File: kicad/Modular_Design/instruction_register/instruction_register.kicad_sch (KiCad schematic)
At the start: 7 parts

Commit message: PD 70% impl
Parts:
- added J?: /implied, symbol Connector_Generic:Conn_01x01
- added J?: d, symbol Connector_Generic:Conn_01x08
- added J?: 0/ir, symbol Connector_Generic:Conn_01x01
- added J?: /twocycle, symbol Connector_Generic:Conn_01x01
- added U?: 4002, symbol 4xxx:4002
- added U? (x3): 74LS27, symbol 74xx:74LS27
- added U? (x6): 74LS04, symbol 74xx:74LS04
- added U?: 74AHC240, symbol 74xx:74AHC240
- added U?: 4081, symbol 4xxx:4081
- added U?: 4011, symbol 4xxx:4011
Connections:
- net GND: now also U?.10 (GND), U?.1 (1OE), U?.10 (GND), U?.19 (2OE)
- net at U?.1 (OE): now also J?.1 (Pin_1)
- net at U?.11 (Load): now also J?.1 (Pin_1)
- net at U?.12 (Q7): now also U?.1, U?.11 (2A3), U?.13
- net at U?.13 (Q6): now also U?.13 (2A2)
- net at U?.14 (Q5): now also U?.15 (2A1)
- net at U?.15 (Q4): now also U?.17 (2A0), U?.2, U?.5
- net at U?.16 (Q3): now also U?.1, U?.1, U?.8 (1A3)
- net at U?.17 (Q2): now also U?.2, U?.3, U?.6 (1A2)
- net at U?.18 (Q1): now also U?.1, U?.4 (1A1)
- net at U?.19 (Q0): now also U?.1, U?.1, U?.2 (1A0)
- net at U?.2 (D0): now also J?.1 (Pin_1)
- net +5V: now reaches U?.20 (VCC)
- net +5V: now also U?.20 (VCC), U?.20 (VCC)
- net at U?.3 (D1): now also J?.2 (Pin_2)
- net at U?.4 (D2): now also J?.3 (Pin_3)
- net at U?.5 (D3): now also J?.4 (Pin_4)
- net at U?.6 (D4): now also J?.5 (Pin_5)
- net at U?.7 (D5): now also J?.6 (Pin_6)
- net at U?.8 (D6): now also J?.7 (Pin_7)
- net at U?.9 (D7): now also J?.8 (Pin_8)
- net at U?.2 (D0): now also U?.18 (1Y0)
- net at U?.3 (D1): now also U?.16 (1Y1)
- net at U?.4 (D2): now also U?.14 (1Y2)
- net at U?.5 (D3): now also U?.12 (1Y3)
- net at U?.6 (D4): now also U?.3 (2Y0)
- net at U?.7 (D5): now also U?.5 (2Y1)
- net at U?.8 (D6): now also U?.7 (2Y2)
- net at U?.9 (D7): now also U?.9 (2Y3)
- new net: U?.1, U?.1
- new net: U?.2, U?.2 (x2)
- new net: U?.2, U?.4
- new net: J?.1 (Pin_1), U?.2
- new net: U?.1, U?.12
- new net: U?.1, U?.1, U?.12
- new net: U?.13, U?.2
- new net: U?.1, U?.3
- new net: J?.1 (Pin_1), U?.3
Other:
- moved on the sheet: J?, U?, U?A

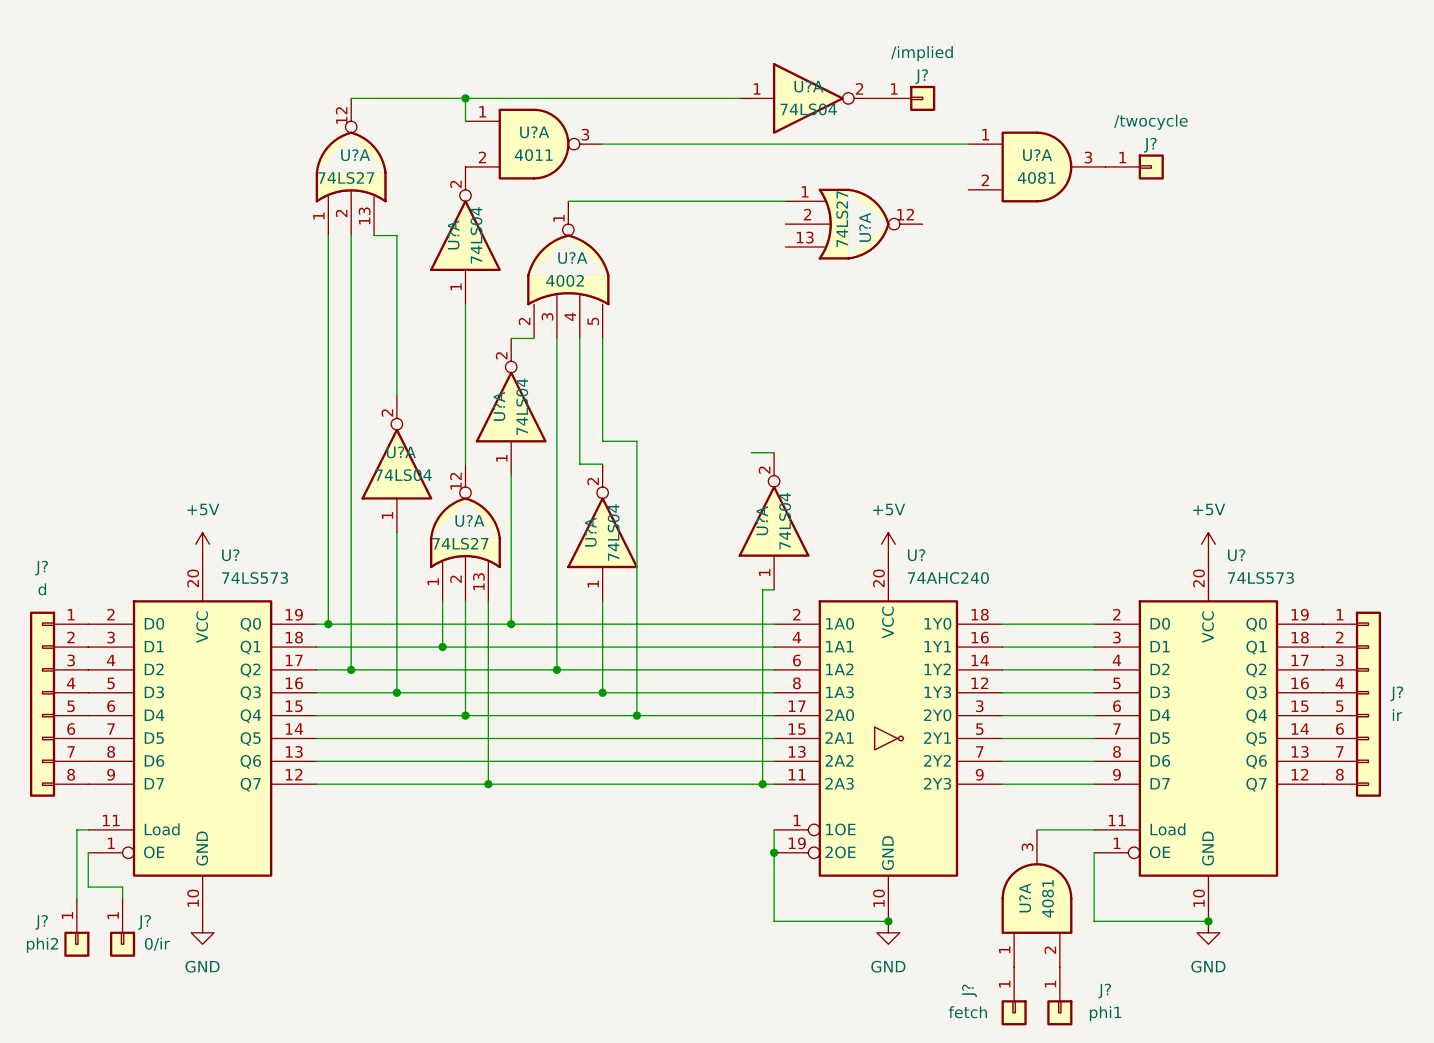
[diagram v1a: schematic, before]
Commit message: finish logic gates between ir and predecoder
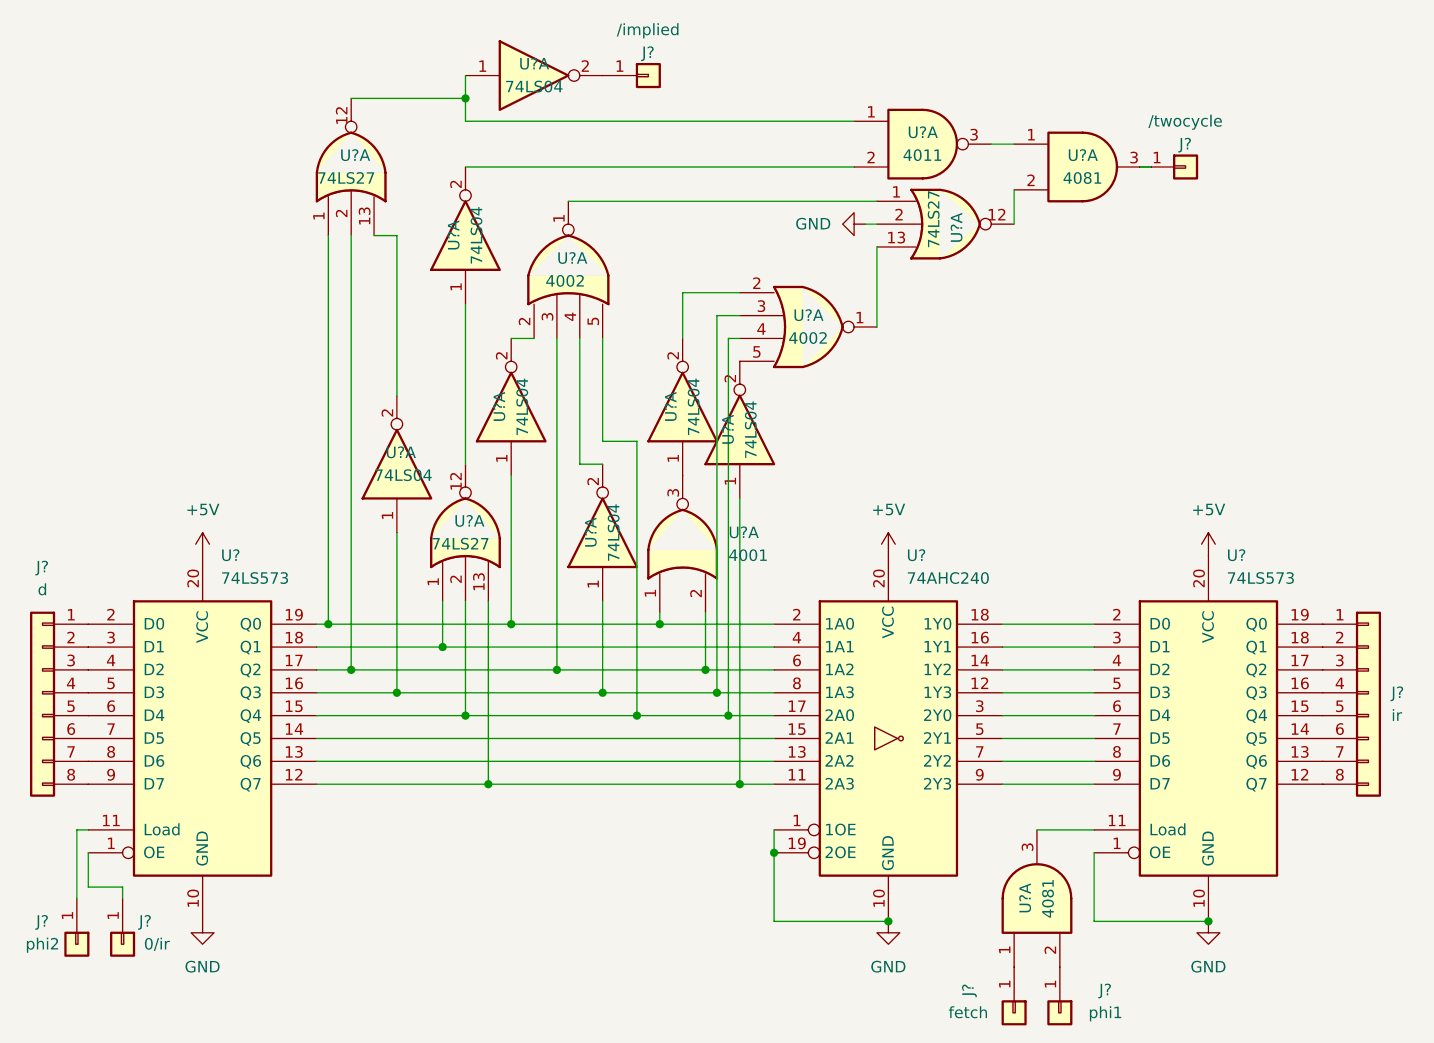
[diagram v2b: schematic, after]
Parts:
- removed U?: 74LS04, symbol 74xx:74LS04
- added U? (x2): 74LS04, symbol 74xx:74LS04
- added U?: 4002, symbol 4xxx:4002
- added U?: 4001, symbol 4xxx:4001
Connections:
- net GND: now also U?.2
- net at U?.17 (Q2), U?.2, U?.3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: now also U?.2
- net at U?.15 (Q4), U?.17 (2A0), U?.2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: now also U?.4
- net at U?.11 (2A3), U?.12 (Q7), U?.13: now also U?.1
- net at U?.1, U?.1, U?.19 (Q0)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: now also U?.1
- net at U?.12: now also U?.2
- net at U?.13: now also U?.1
- net at U?.1, U?.1, U?.16 (Q3)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: now also U?.3
- new net: U?.2, U?.5
- new net: U?.1, U?.3
- new net: U?.2, U?.2
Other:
- moved on the sheet: J?, U?A
